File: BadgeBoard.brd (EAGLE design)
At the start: 70 x 30 mm, 15 parts

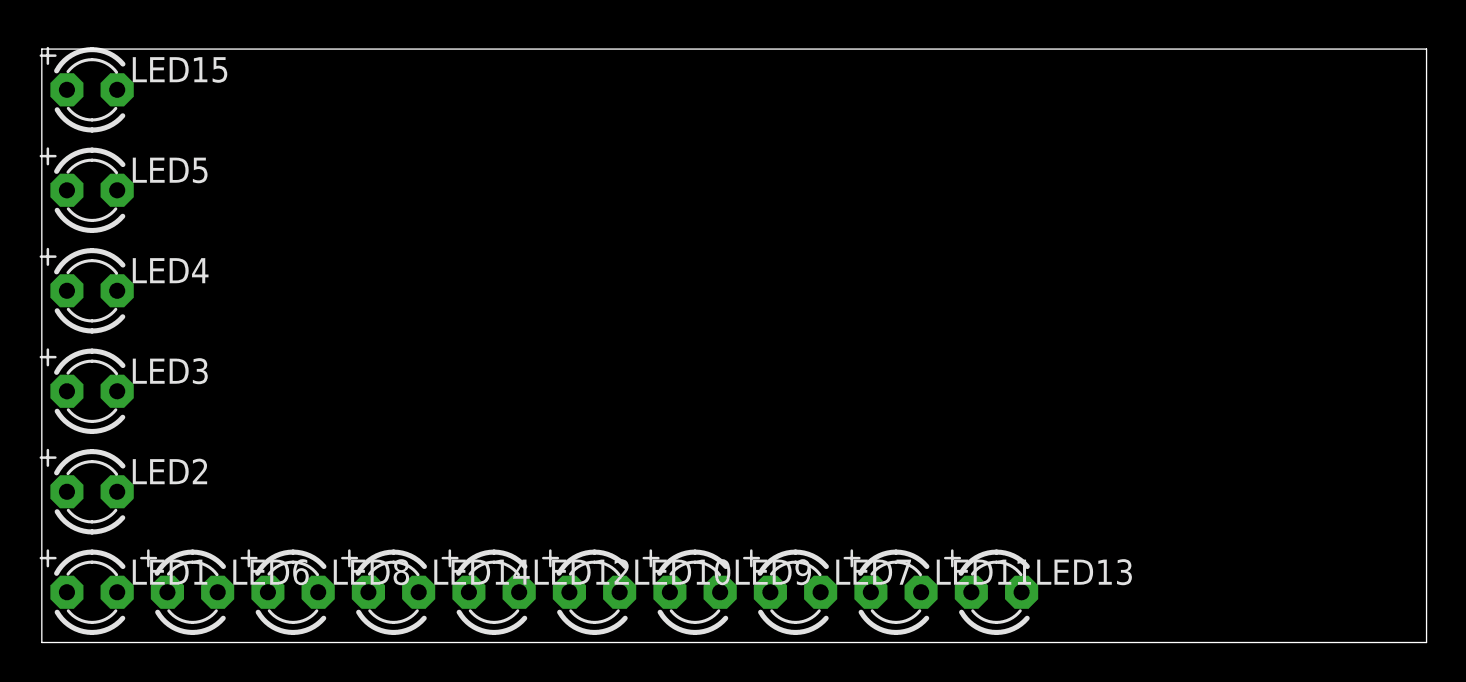
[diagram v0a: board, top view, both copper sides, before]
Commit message: update led matrix
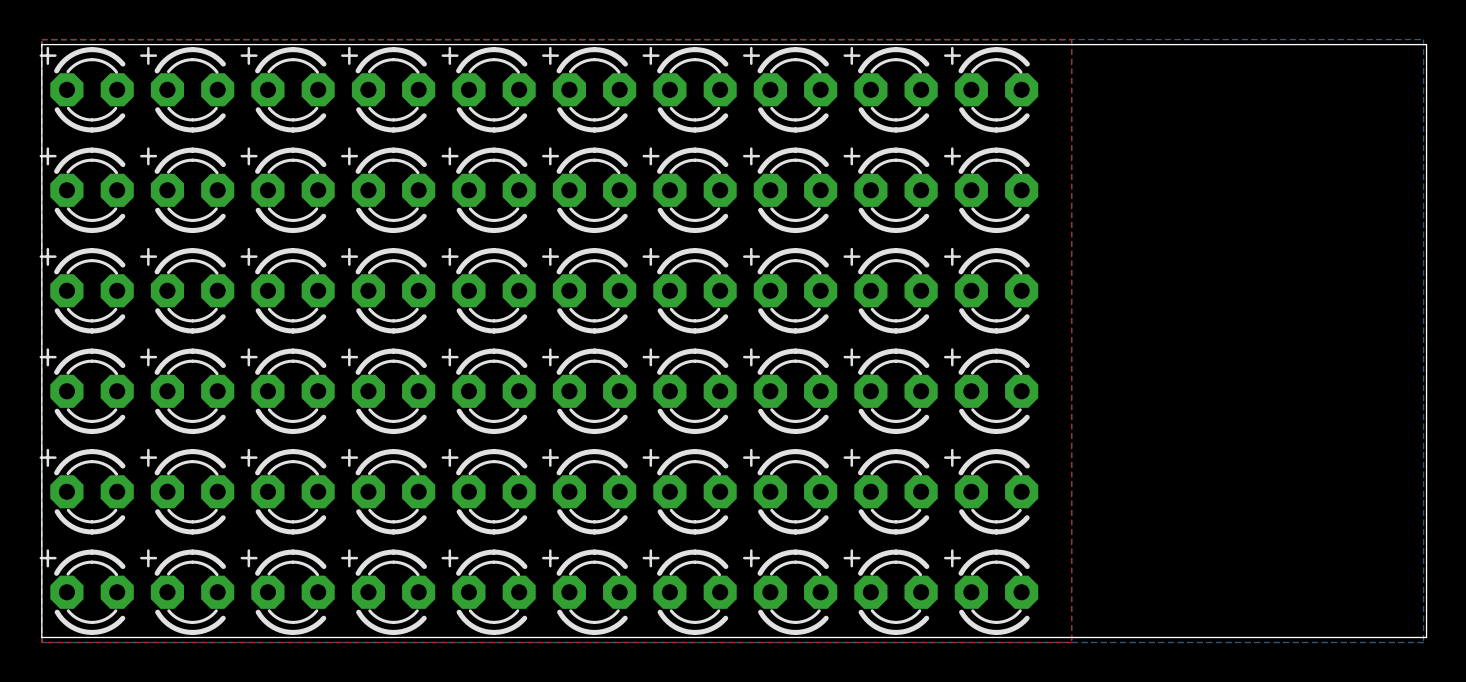
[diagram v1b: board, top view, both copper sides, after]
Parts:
- added LED16, LED17, LED18, LED19, LED20, LED21, LED22, LED23, LED24, LED25, LED26, LED27, LED28, LED29, LED30, LED31, LED32, LED33, LED34, LED35, LED36, LED37, LED38, LED39, LED40, LED41, LED42, LED43, LED44, LED45, LED46, LED47, LED48, LED49, LED50, LED51, LED52, LED53, LED54, LED55, LED56, LED57, LED58, LED59, LED60: (no value), adafruit:LED3MM
- moved LED7 30.5 mm to (7.62, 2.54)
- moved LED13 30.5 mm to (17.8, 2.54)
- moved LED10 28.7 mm to (7.62, 22.9)
- moved LED14 27.4 mm to (7.62, 27.9)
- moved LED6 25.9 mm to (2.54, 27.9)
- moved LED9 20.3 mm to (12.7, 2.54)
- moved LED11 20.3 mm to (22.9, 2.54)
- moved LED12 18.3 mm to (7.62, 12.7)
- moved LED15 11.4 mm to (7.62, 17.8)
- moved LED8 7.18 mm to (7.62, 7.62)
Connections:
- new net GND: LED10.K, LED11.K, LED12.K, LED7.K, LED8.K, LED9.K
- new net VLED: LED10.A, LED11.A, LED12.A, LED7.A, LED8.A, LED9.A
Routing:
- added copper zone on layer 16, net GND
- added copper zone on layer 1, net VLED

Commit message: More layout
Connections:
- net GND: now also LED1.K, LED13.K, LED14.K, LED15.K, LED16.K, LED17.K, LED18.K, LED19.K, LED2.K, LED20.K, LED21.K, LED22.K, LED23.K, LED24.K, LED25.K, LED26.K, LED27.K, LED28.K, LED29.K, LED3.K, LED30.K, LED31.K, LED32.K, LED33.K, LED34.K, LED35.K, LED36.K, LED37.K, LED38.K, LED39.K, LED4.K, LED40.K, LED41.K, LED42.K, LED43.K, LED44.K, LED45.K, LED46.K, LED47.K, LED48.K, LED49.K, LED5.K, LED50.K, LED51.K, LED52.K, LED53.K, LED54.K, LED55.K, LED56.K, LED57.K, LED58.K, LED59.K, LED6.K, LED60.K
- net VLED: now also LED1.A, LED13.A, LED14.A, LED15.A, LED16.A, LED17.A, LED18.A, LED19.A, LED2.A, LED20.A, LED21.A, LED22.A, LED23.A, LED24.A, LED25.A, LED26.A, LED27.A, LED28.A, LED29.A, LED3.A, LED30.A, LED31.A, LED32.A, LED33.A, LED34.A, LED35.A, LED36.A, LED37.A, LED38.A, LED39.A, LED4.A, LED40.A, LED41.A, LED42.A, LED43.A, LED44.A, LED45.A, LED46.A, LED47.A, LED48.A, LED49.A, LED5.A, LED50.A, LED51.A, LED52.A, LED53.A, LED54.A, LED55.A, LED56.A, LED57.A, LED58.A, LED59.A, LED6.A, LED60.A
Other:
- outline, holes or cut-outs redrawn
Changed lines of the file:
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@@
 <layer number="43" name="vRestrict" color="2" fill="10" visible="yes" active="yes"/>
 <layer number="44" name="Drills" color="7" fill="1" visible="no" active="yes"/>
-<layer number="45" name="Holes" color="7" fill="1" visible="no" active="yes"/>
-<layer number="46" name="Milling" color="3" fill="1" visible="no" active="yes"/>
+<layer number="45" name="Holes" color="7" fill="1" visible="yes" active="yes"/>
+<layer number="46" name="Milling" color="3" fill="1" visible="yes" active="yes"/>
 <layer number="47" name="Measures" color="7" fill="1" visible="no" active="yes"/>
 <layer number="48" name="Document" color="7" fill="1" visible="yes" active="yes"/>
@@
 <board>
 <plain>
-<wire x1="0" y1="0.254" x2="70" y2="0.254" width="0" layer="20"/>
-<wire x1="70" y1="0.254" x2="70" y2="30.226" width="0" layer="20"/>
-<wire x1="70" y1="30.226" x2="0" y2="30.226" width="0" layer="20"/>
-<wire x1="0" y1="30.226" x2="0" y2="0.254" width="0" layer="20"/>
+<wire x1="62.5" y1="30.226" x2="2" y2="30.226" width="0" layer="20"/>
+<wire x1="2" y1="30.226" x2="0" y2="28.226" width="0" layer="20" curve="90"/>
+<wire x1="0" y1="28.226" x2="0" y2="2.254" width="0" layer="20"/>
+<wire x1="0" y1="2.254" x2="2" y2="0.254" width="0" layer="20" curve="90"/>
+<wire x1="2" y1="0.254" x2="62.5" y2="0.254" width="0" layer="20"/>
+<wire x1="62.5" y1="0.254" x2="70" y2="7.754" width="0" layer="20" curve="90"/>
+<wire x1="70" y1="7.754" x2="70" y2="22.726" width="0" layer="20"/>
+<wire x1="70" y1="22.726" x2="62.5" y2="30.226" width="0" layer="20" curve="90"/>
+<circle x="64.77" y="25.4" radius="2.54" width="0.4064" layer="20"/>
 </plain>
 <attributes>
@@
 <vertex x="0" y="0"/>
 </polygon>
+<contactref element="LED6" pad="A"/>
+<contactref element="LED5" pad="A"/>
+<contactref element="LED4" pad="A"/>
+<contactref element="LED3" pad="A"/>
+<contactref element="LED2" pad="A"/>
+<contactref element="LED1" pad="A"/>
+<contactref element="LED18" pad="A"/>
+<contactref element="LED17" pad="A"/>
+<contactref element="LED16" pad="A"/>
+<contactref element="LED15" pad="A"/>
+<contactref element="LED14" pad="A"/>
+<contactref element="LED13" pad="A"/>
+<contactref element="LED19" pad="A"/>
+<contactref element="LED20" pad="A"/>
+<contactref element="LED21" pad="A"/>
+<contactref element="LED22" pad="A"/>
+<contactref element="LED23" pad="A"/>
+<contactref element="LED24" pad="A"/>
+<contactref element="LED30" pad="A"/>
+<contactref element="LED29" pad="A"/>
+<contactref element="LED28" pad="A"/>
+<contactref element="LED27" pad="A"/>
+<contactref element="LED26" pad="A"/>
+<contactref element="LED25" pad="A"/>
+<contactref element="LED31" pad="A"/>
+<contactref element="LED32" pad="A"/>
+<contactref element="LED33" pad="A"/>
+<contactref element="LED34" pad="A"/>
+<contactref element="LED35" pad="A"/>
+<contactref element="LED36" pad="A"/>
+<contactref element="LED42" pad="A"/>
+<contactref element="LED41" pad="A"/>
+<contactref element="LED40" pad="A"/>
+<contactref element="LED39" pad="A"/>
+<contactref element="LED38" pad="A"/>
+<contactref element="LED37" pad="A"/>
+<contactref element="LED43" pad="A"/>
+<contactref element="LED44" pad="A"/>
+<contactref element="LED45" pad="A"/>
+<contactref element="LED46" pad="A"/>
+<contactref element="LED47" pad="A"/>
+<contactref element="LED48" pad="A"/>
+<contactref element="LED54" pad="A"/>
+<contactref element="LED53" pad="A"/>
+<contactref element="LED52" pad="A"/>
+<contactref element="LED51" pad="A"/>
+<contactref element="LED50" pad="A"/>
+<contactref element="LED49" pad="A"/>
+<contactref element="LED55" pad="A"/>
+<contactref element="LED56" pad="A"/>
+<contactref element="LED57" pad="A"/>
+<contactref element="LED58" pad="A"/>
+<contactref element="LED59" pad="A"/>
+<contactref element="LED60" pad="A"/>
 </signal>
 <signal name="GND">
@@
 <vertex x="0" y="0"/>
 </polygon>
+<contactref element="LED6" pad="K"/>
+<contactref element="LED5" pad="K"/>
+<contactref element="LED4" pad="K"/>
+<contactref element="LED3" pad="K"/>
+<contactref element="LED2" pad="K"/>
+<contactref element="LED1" pad="K"/>
+<contactref element="LED18" pad="K"/>
+<contactref element="LED17" pad="K"/>
+<contactref element="LED16" pad="K"/>
+<contactref element="LED15" pad="K"/>
+<contactref element="LED14" pad="K"/>
+<contactref element="LED13" pad="K"/>
+<contactref element="LED19" pad="K"/>
+<contactref element="LED20" pad="K"/>
+<contactref element="LED21" pad="K"/>
+<contactref element="LED22" pad="K"/>
+<contactref element="LED23" pad="K"/>
+<contactref element="LED24" pad="K"/>
+<contactref element="LED30" pad="K"/>
+<contactref element="LED29" pad="K"/>
+<contactref element="LED28" pad="K"/>
+<contactref element="LED27" pad="K"/>
+<contactref element="LED26" pad="K"/>
+<contactref element="LED25" pad="K"/>
+<contactref element="LED31" pad="K"/>
+<contactref element="LED32" pad="K"/>
+<contactref element="LED33" pad="K"/>
+<contactref element="LED34" pad="K"/>
+<contactref element="LED35" pad="K"/>
+<contactref element="LED36" pad="K"/>
+<contactref element="LED42" pad="K"/>
+<contactref element="LED41" pad="K"/>
+<contactref element="LED40" pad="K"/>
+<contactref element="LED39" pad="K"/>
+<contactref element="LED38" pad="K"/>
+<contactref element="LED37" pad="K"/>
+<contactref element="LED43" pad="K"/>
+<contactref element="LED44" pad="K"/>
+<contactref element="LED45" pad="K"/>
+<contactref element="LED46" pad="K"/>
+<contactref element="LED47" pad="K"/>
+<contactref element="LED48" pad="K"/>
+<contactref element="LED54" pad="K"/>
+<contactref element="LED53" pad="K"/>
+<contactref element="LED52" pad="K"/>
+<contactref element="LED51" pad="K"/>
+<contactref element="LED50" pad="K"/>
+<contactref element="LED49" pad="K"/>
+<contactref element="LED55" pad="K"/>
+<contactref element="LED56" pad="K"/>
+<contactref element="LED57" pad="K"/>
+<contactref element="LED58" pad="K"/>
+<contactref element="LED59" pad="K"/>
+<contactref element="LED60" pad="K"/>
 </signal>
 </signals>

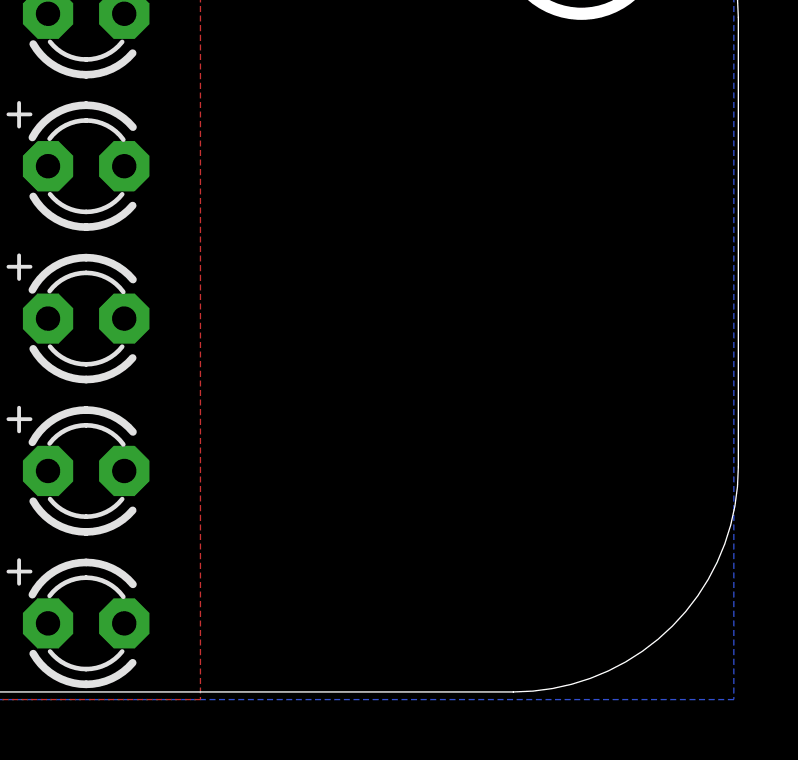
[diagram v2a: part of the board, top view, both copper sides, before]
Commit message: Add logos
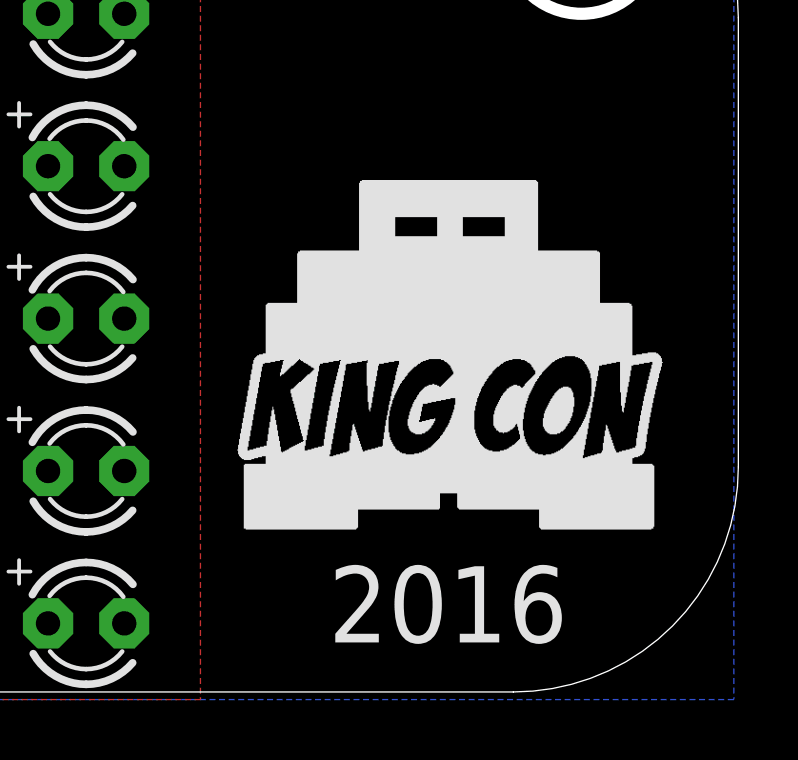
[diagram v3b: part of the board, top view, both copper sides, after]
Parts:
- added U$1: (no value), KingCon_Logo:KINGCON_LOGO_L
- added U$2: (no value), logos:MAKERSPACE_LOGO_FULL_M
- added U$3: (no value), logos:KINGCON_LOGO_L
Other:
- board text added: "2016"
- board text added: "KingCon 2016"
- board text added: "www.kingcon.co.uk"
- board text added: "www.makerspace.org.uk"
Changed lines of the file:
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@@
 <wire x1="70" y1="22.726" x2="62.5" y2="30.226" width="0" layer="20" curve="90"/>
 <circle x="64.77" y="25.4" radius="2.54" width="0.4064" layer="20"/>
+<text x="60.325" y="3.175" size="2.54" layer="25" font="vector" align="center">2016</text>
+<text x="26.67" y="25.4" size="3.81" layer="26" rot="MR0" align="center">KingCon 2016</text>
+<text x="38.1" y="5.08" size="1.27" layer="26" font="vector" rot="MR0" align="center">www.kingcon.co.uk</text>
+<text x="17.145" y="5.08" size="1.27" layer="26" font="vector" rot="MR0" align="center">www.makerspace.org.uk</text>
 </plain>
 <attributes>
@@
 <attribute name="VALUE" x="45.085" y="0.889" size="1.27" layer="27" ratio="10"/>
 </element>
+<element name="U$1" library="KingCon_Logo" package="KINGCON_LOGO_L" value="" x="52.705" y="3.81"/>
+<element name="U$2" library="logos" package="MAKERSPACE_LOGO_FULL_M" value="" x="26.67" y="7.62" rot="MR0"/>
+<element name="U$3" library="logos" package="KINGCON_LOGO_L" value="" x="45.72" y="5.08" rot="MR0"/>
 </elements>
 <signals>

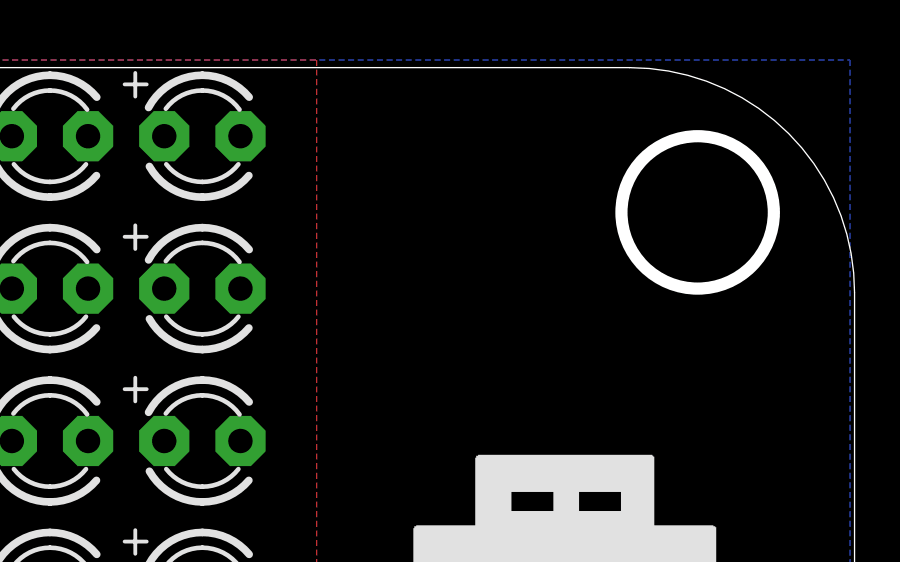
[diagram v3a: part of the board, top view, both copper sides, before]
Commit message: add switch and i-lim res
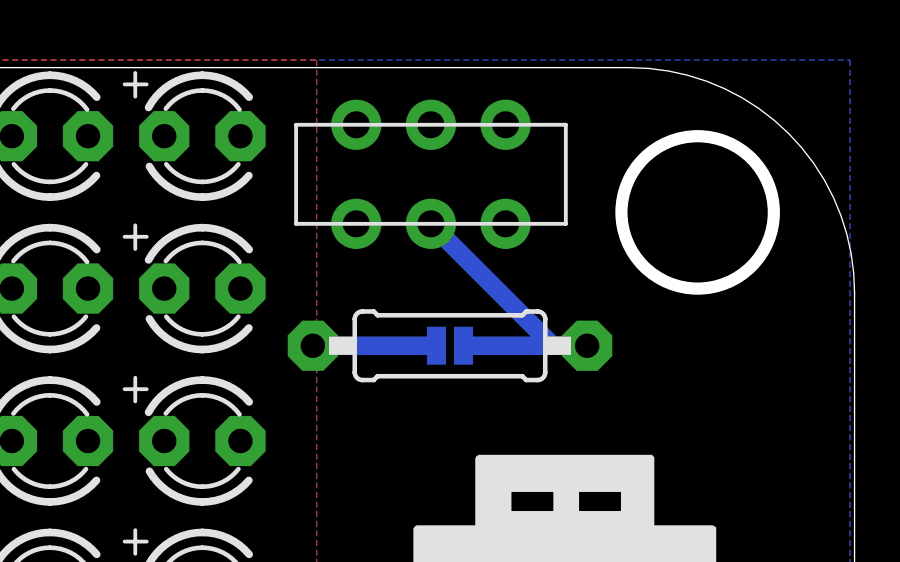
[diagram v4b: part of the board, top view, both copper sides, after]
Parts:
- added JP1: JUMPER-PAD-2-NO, SparkFun-Passives:PAD-JUMPER-2-NO_NO_SILK
- added R1: (no value), adafruit:0207/9
- added U$4: JS202011CQN, switch:JS202011CQN
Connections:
- new net SW_BATT: JP1.1, R1.1, U$4.2
- new net VBATT: U$4.3
- net VLED: now also JP1.2, R1.2
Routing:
- net SW_BATT: track 0.00 -> 11.0 mm
- net VLED: track 0.00 -> 4.12 mm
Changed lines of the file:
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@@
 <element name="U$2" library="logos" package="MAKERSPACE_LOGO_FULL_M" value="" x="26.67" y="7.62" rot="MR0"/>
 <element name="U$3" library="logos" package="KINGCON_LOGO_L" value="" x="45.72" y="5.08" rot="MR0"/>
+<element name="U$4" library="switch" package="JS202011CQN" value="JS202011CQN" x="55.88" y="26.67" smashed="yes"/>
+<element name="R1" library="adafruit" package="0207/9" value="" x="56.515" y="20.955" smashed="yes" rot="R180">
+<attribute name="VALUE" x="58.7756" y="21.59" size="1.27" layer="27" ratio="10" rot="R180"/>
+</element>
+<element name="JP1" library="SparkFun-Passives" package="PAD-JUMPER-2-NO_NO_SILK" value="JUMPER-PAD-2-NO" x="56.515" y="20.955" smashed="yes" rot="MR0"/>
 </elements>
 <signals>
@@
 <contactref element="LED9" pad="A"/>
 <contactref element="LED8" pad="A"/>
-<polygon width="0.4064" layer="1">
+<polygon width="0.6096" layer="1">
 <vertex x="0" y="30.48"/>
 <vertex x="52.07" y="30.48"/>
@@
 <contactref element="LED59" pad="A"/>
 <contactref element="LED60" pad="A"/>
+<contactref element="R1" pad="2"/>
+<contactref element="JP1" pad="2"/>
+<wire x1="56.065" y1="20.955" x2="51.943" y2="20.955" width="0.6096" layer="16"/>
+<wire x1="1.27" y1="22.86" x2="1.27" y2="27.94" width="0" layer="19" extent="1-1"/>
+<wire x1="1.27" y1="17.78" x2="1.27" y2="22.86" width="0" layer="19" extent="1-1"/>
+<wire x1="1.27" y1="12.7" x2="1.27" y2="17.78" width="0" layer="19" extent="1-1"/>
+<wire x1="1.27" y1="7.62" x2="1.27" y2="12.7" width="0" layer="19" extent="1-1"/>
+<wire x1="1.27" y1="2.54" x2="1.27" y2="7.62" width="0" layer="19" extent="1-1"/>
+<wire x1="6.35" y1="27.94" x2="1.27" y2="27.94" width="0" layer="19" extent="1-1"/>
 </signal>
 <signal name="GND">
@@
 <contactref element="LED60" pad="K"/>
 </signal>
+<signal name="SW_BATT">
+<contactref element="U$4" pad="2"/>
+<contactref element="R1" pad="1"/>
+<contactref element="JP1" pad="1"/>
+<wire x1="61.087" y1="20.955" x2="56.965" y2="20.955" width="0.6096" layer="16"/>
+<wire x1="55.88" y1="25.019" x2="59.944" y2="20.955" width="0.6096" layer="16"/>
+<wire x1="59.944" y1="20.955" x2="61.087" y2="20.955" width="0.6096" layer="16"/>
+</signal>
+<signal name="VBATT">
+<contactref element="U$4" pad="3"/>
+</signal>
 </signals>
